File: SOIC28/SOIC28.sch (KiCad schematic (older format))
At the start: 4 parts, among them J1 Conn_01x14, J2 Conn_02x14_Counter_Clockwise, J3 Conn_01x14, J4 Conn_02x14_Counter_Clockwise

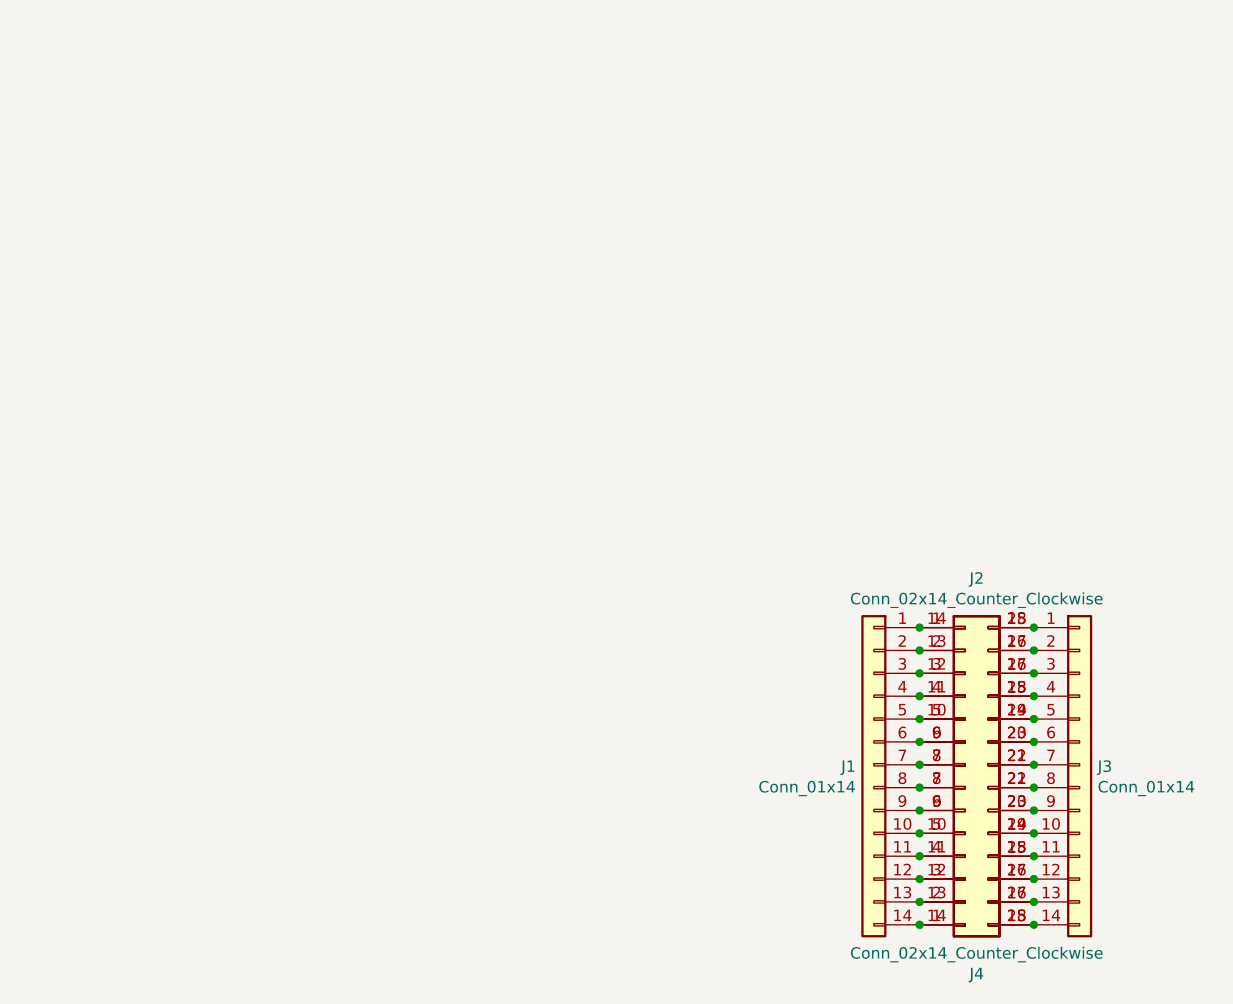
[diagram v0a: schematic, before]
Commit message: USB, SD and CR Cells Added
MicroSD, MicroUSB, MiniUSB, USB-C, CR1220, CR2032 added as well as all schematics page sizes optimised
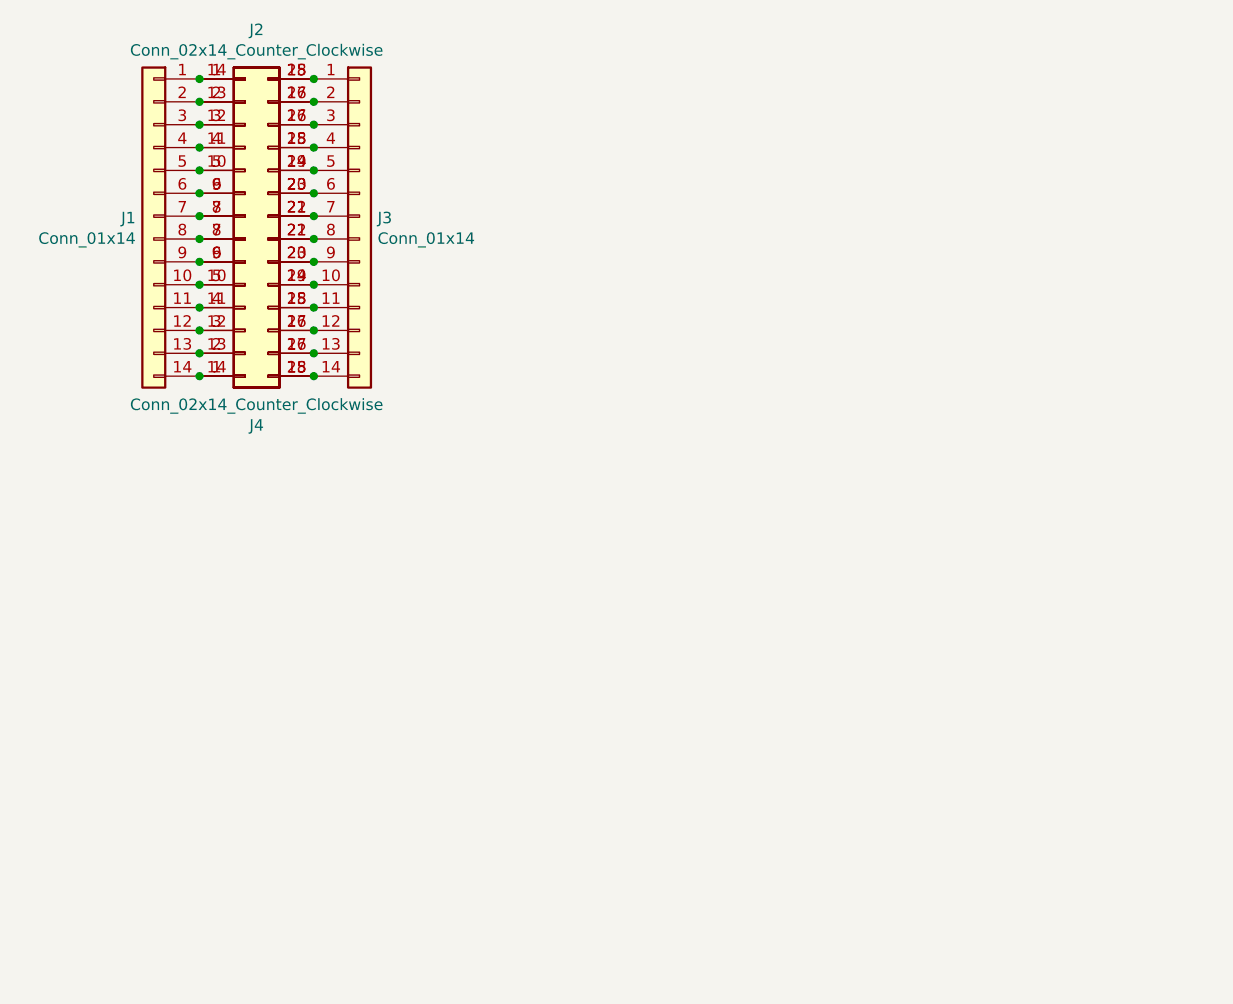
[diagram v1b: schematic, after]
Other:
- moved on the sheet: J1, J2, J3, J4
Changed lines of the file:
@@
 EESchema Schematic File Version 4
+LIBS:SOIC28-cache
 EELAYER 29 0
 EELAYER END
-$Descr A4 11693 8268
+$Descr User 5197 4016
 encoding utf-8
 Sheet 1 1
-Title ""
-Date ""
-Rev ""
-Comp ""
-Comment1 ""
-Comment2 ""
-Comment3 ""
+Title "SOIC28 To DIP28 Breakout Board"
+Date "2019-07-10"
+Rev "1"
+Comp "SirBoard"
+Comment1 "SOIC28 P = 1.27mm"
+Comment2 "TSSOP28 P = 0.65mm"
+Comment3 "DIP28 P = 2.54mm"
 Comment4 ""
 $EndDescr
@@
 L Connector_Generic:Conn_01x14 J1
 U 1 1 5D2A30AE
-P 5200 3750
-F 0 "J1" H 5279 3742 50  0000 L CNN
-F 1 "Conn_01x14" H 5279 3652 50  0000 L CNN
-F 2 "Connector_PinHeader_2.54mm:PinHeader_1x14_P2.54mm_Vertical" H 5200 3750 50  0001 C CNN
-F 3 "~" H 5200 3750 50  0001 C CNN
-	1    5200 3750
+P 2050 1350
+F 0 "J1" H 2129 1342 50  0000 L CNN
+F 1 "Conn_01x14" H 2129 1252 50  0000 L CNN
+F 2 "Connector_PinHeader_2.54mm:PinHeader_1x14_P2.54mm_Vertical" H 2050 1350 50  0001 C CNN
+F 3 "~" H 2050 1350 50  0001 C CNN
+	1    2050 1350
 	-1   0    0    -1
 $EndComp
@@
 L Connector_Generic:Conn_01x14 J3
 U 1 1 5D2A49D3
-P 6100 3750
-F 0 "J3" H 6179 3742 50  0000 L CNN
-F 1 "Conn_01x14" H 6179 3652 50  0000 L CNN
-F 2 "Connector_PinHeader_2.54mm:PinHeader_1x14_P2.54mm_Vertical" H 6100 3750 50  0001 C CNN
-F 3 "~" H 6100 3750 50  0001 C CNN
-	1    6100 3750
+P 2950 1350
+F 0 "J3" H 3029 1342 50  0000 L CNN
+F 1 "Conn_01x14" H 3029 1252 50  0000 L CNN
+F 2 "Connector_PinHeader_2.54mm:PinHeader_1x14_P2.54mm_Vertical" H 2950 1350 50  0001 C CNN
+F 3 "~" H 2950 1350 50  0001 C CNN
+	1    2950 1350
 	1    0    0    -1
 $EndComp
@@
 L Connector_Generic:Conn_02x14_Counter_Clockwise J2
 U 1 1 5D2A245F
-P 5600 3750
-F 0 "J2" H 5650 4565 50  0000 C CNN
-F 1 "Conn_02x14_Counter_Clockwise" H 5650 4475 50  0000 C CNN
-F 2 "Package_SO:SOIC-28W_7.5x18.7mm_P1.27mm" H 5600 3750 50  0001 C CNN
-F 3 "~" H 5600 3750 50  0001 C CNN
-	1    5600 3750
+P 2450 1350
+F 0 "J2" H 2500 2165 50  0000 C CNN
+F 1 "Conn_02x14_Counter_Clockwise" H 2500 2075 50  0000 C CNN
+F 2 "Package_SO:SOIC-28W_7.5x18.7mm_P1.27mm" H 2450 1350 50  0001 C CNN
+F 3 "~" H 2450 1350 50  0001 C CNN
+	1    2450 1350
 	1    0    0    -1
 $EndComp
@@
 L Connector_Generic:Conn_02x14_Counter_Clockwise J4
 U 1 1 5D2AC70C
-P 5600 3850
-F 0 "J4" H 5650 4665 50  0000 C CNN
-F 1 "Conn_02x14_Counter_Clockwise" H 5650 4575 50  0000 C CNN
-F 2 "Package_SO:TSSOP-28_4.4x9.7mm_P0.65mm" H 5600 3850 50  0001 C CNN
-F 3 "~" H 5600 3850 50  0001 C CNN
-	1    5600 3850
+P 2450 1450
+F 0 "J4" H 2500 2265 50  0000 C CNN
+F 1 "Conn_02x14_Counter_Clockwise" H 2500 2175 50  0000 C CNN
+F 2 "Package_SO:TSSOP-28_4.4x9.7mm_P0.65mm" H 2450 1450 50  0001 C CNN
+F 3 "~" H 2450 1450 50  0001 C CNN
+	1    2450 1450
 	1    0    0    1
 $EndComp
-Connection ~ 5400 3150
-Connection ~ 5400 3250
-Connection ~ 5400 3350
-Connection ~ 5400 3450
-Connection ~ 5400 3550
-Connection ~ 5400 3650
-Connection ~ 5400 3750
-Connection ~ 5400 3850
-Connection ~ 5400 3950
-Connection ~ 5400 4050
-Connection ~ 5400 4150
-Connection ~ 5400 4250
-Connection ~ 5400 4350
-Connection ~ 5400 4450
-Connection ~ 5900 3150
-Connection ~ 5900 3250
-Connection ~ 5900 3350
-Connection ~ 5900 3450
-Connection ~ 5900 3550
-Connection ~ 5900 3650
-Connection ~ 5900 3750
-Connection ~ 5900 3850
-Connection ~ 5900 3950
-Connection ~ 5900 4050
-Connection ~ 5900 4150
-Connection ~ 5900 4250
-Connection ~ 5900 4350
-Connection ~ 5900 4450
+Connection ~ 2250 750
+Connection ~ 2250 850
+Connection ~ 2250 950
+Connection ~ 2250 1050
+Connection ~ 2250 1150
+Connection ~ 2250 1250
+Connection ~ 2250 1350
+Connection ~ 2250 1450
+Connection ~ 2250 1550
+Connection ~ 2250 1650
+Connection ~ 2250 1750
+Connection ~ 2250 1850
+Connection ~ 2250 1950
+Connection ~ 2250 2050
+Connection ~ 2750 750
+Connection ~ 2750 850
+Connection ~ 2750 950
+Connection ~ 2750 1050
+Connection ~ 2750 1150
+Connection ~ 2750 1250
+Connection ~ 2750 1350
+Connection ~ 2750 1450
+Connection ~ 2750 1550
+Connection ~ 2750 1650
+Connection ~ 2750 1750
+Connection ~ 2750 1850
+Connection ~ 2750 1950
+Connection ~ 2750 2050
 $EndSCHEMATC

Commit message: Schematic PDF and 3D Renders added
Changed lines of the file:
@@
 P 2050 1350
 F 0 "J1" H 2129 1342 50  0000 L CNN
-F 1 "Conn_01x14" H 2129 1252 50  0000 L CNN
+F 1 "Conn_01x14" H 2129 1252 50  0001 L CNN
 F 2 "Connector_PinHeader_2.54mm:PinHeader_1x14_P2.54mm_Vertical" H 2050 1350 50  0001 C CNN
 F 3 "~" H 2050 1350 50  0001 C CNN
@@
 P 2950 1350
 F 0 "J3" H 3029 1342 50  0000 L CNN
-F 1 "Conn_01x14" H 3029 1252 50  0000 L CNN
+F 1 "Conn_01x14" H 3029 1252 50  0001 L CNN
 F 2 "Connector_PinHeader_2.54mm:PinHeader_1x14_P2.54mm_Vertical" H 2950 1350 50  0001 C CNN
 F 3 "~" H 2950 1350 50  0001 C CNN
@@
 P 2450 1350
 F 0 "J2" H 2500 2165 50  0000 C CNN
-F 1 "Conn_02x14_Counter_Clockwise" H 2500 2075 50  0000 C CNN
+F 1 "Conn_02x14_Counter_Clockwise" H 2500 2075 50  0001 C CNN
 F 2 "Package_SO:SOIC-28W_7.5x18.7mm_P1.27mm" H 2450 1350 50  0001 C CNN
 F 3 "~" H 2450 1350 50  0001 C CNN
@@
 P 2450 1450
 F 0 "J4" H 2500 2265 50  0000 C CNN
-F 1 "Conn_02x14_Counter_Clockwise" H 2500 2175 50  0000 C CNN
+F 1 "Conn_02x14_Counter_Clockwise" H 2500 2175 50  0001 C CNN
 F 2 "Package_SO:TSSOP-28_4.4x9.7mm_P0.65mm" H 2450 1450 50  0001 C CNN
 F 3 "~" H 2450 1450 50  0001 C CNN
